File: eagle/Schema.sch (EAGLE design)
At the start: 28 parts, among them T1 2N2222, T2 2N2222

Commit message: Added a led
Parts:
- added LED2: (no value), led:LED5MM
- added R21: (no value), rcl:R-EU_0207/10
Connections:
- new net N$26: R21.2, U$1.12
- new net N$27: LED2.A, R21.1
- new net N$28: LED2.C, U$1.13
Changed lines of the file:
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@@
 <part name="R19" library="rcl" library_urn="urn:adsk.eagle:library:334" deviceset="R-EU_" device="0207/10" package3d_urn="urn:adsk.eagle:package:23491/2"/>
 <part name="R20" library="rcl" library_urn="urn:adsk.eagle:library:334" deviceset="R-EU_" device="0207/10" package3d_urn="urn:adsk.eagle:package:23491/2"/>
+<part name="LED2" library="led" library_urn="urn:adsk.eagle:library:259" deviceset="LED" device="5MM" package3d_urn="urn:adsk.eagle:package:15799/2"/>
+<part name="R21" library="rcl" library_urn="urn:adsk.eagle:library:334" deviceset="R-EU_" device="0207/10" package3d_urn="urn:adsk.eagle:package:23491/2"/>
 </parts>
 <sheets>
@@
 <attribute name="NAME" x="-6.35" y="174.2186" size="1.778" layer="95"/>
 <attribute name="VALUE" x="-6.35" y="169.418" size="1.778" layer="96"/>
+</instance>
+<instance part="LED2" gate="G$1" x="68.58" y="83.82" smashed="yes">
+<attribute name="NAME" x="69.596" y="84.328" size="1.778" layer="95" rot="R90"/>
+<attribute name="VALUE" x="74.295" y="79.248" size="1.778" layer="96" rot="R90"/>
+</instance>
+<instance part="R21" gate="G$1" x="73.66" y="88.9" smashed="yes">
+<attribute name="NAME" x="69.85" y="90.3986" size="1.778" layer="95"/>
+<attribute name="VALUE" x="69.85" y="85.598" size="1.778" layer="96"/>
 </instance>
 </instances>
@@
 </segment>
 </net>
+<net name="N$26" class="0">
+<segment>
+<pinref part="U$1" gate="G$1" pin="12"/>
+<pinref part="R21" gate="G$1" pin="2"/>
+<wire x1="86.36" y1="88.9" x2="78.74" y2="88.9" width="0.1524" layer="91"/>
+</segment>
+</net>
+<net name="N$27" class="0">
+<segment>
+<pinref part="R21" gate="G$1" pin="1"/>
+<pinref part="LED2" gate="G$1" pin="A"/>
+<wire x1="68.58" y1="88.9" x2="68.58" y2="86.36" width="0.1524" layer="91"/>
+</segment>
+</net>
+<net name="N$28" class="0">
+<segment>
+<pinref part="U$1" gate="G$1" pin="13"/>
+<wire x1="86.36" y1="86.36" x2="76.2" y2="86.36" width="0.1524" layer="91"/>
+<pinref part="LED2" gate="G$1" pin="C"/>
+<wire x1="76.2" y1="86.36" x2="76.2" y2="78.74" width="0.1524" layer="91"/>
+<wire x1="76.2" y1="78.74" x2="68.58" y2="78.74" width="0.1524" layer="91"/>
+</segment>
+</net>

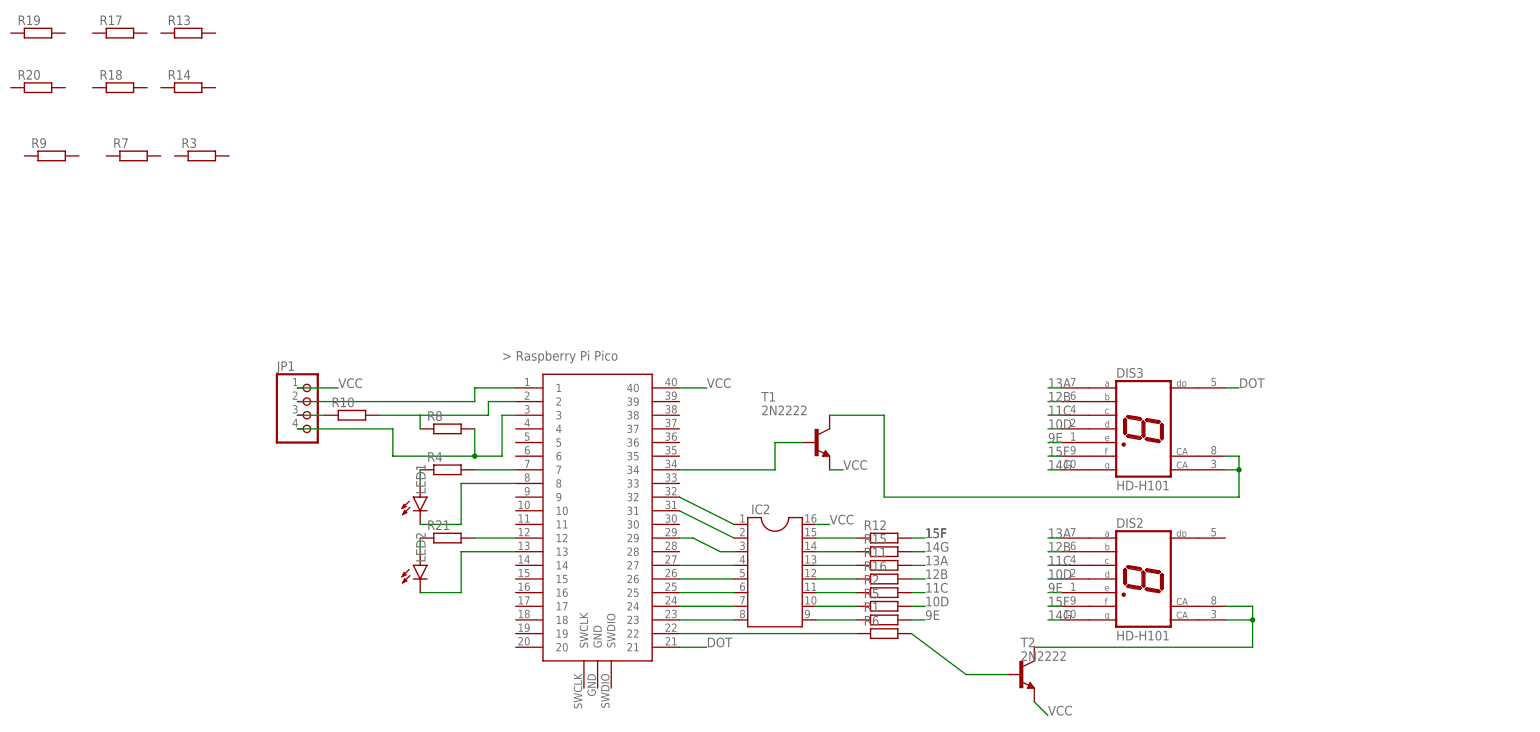
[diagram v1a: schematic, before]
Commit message: [FIX] eagle schéma
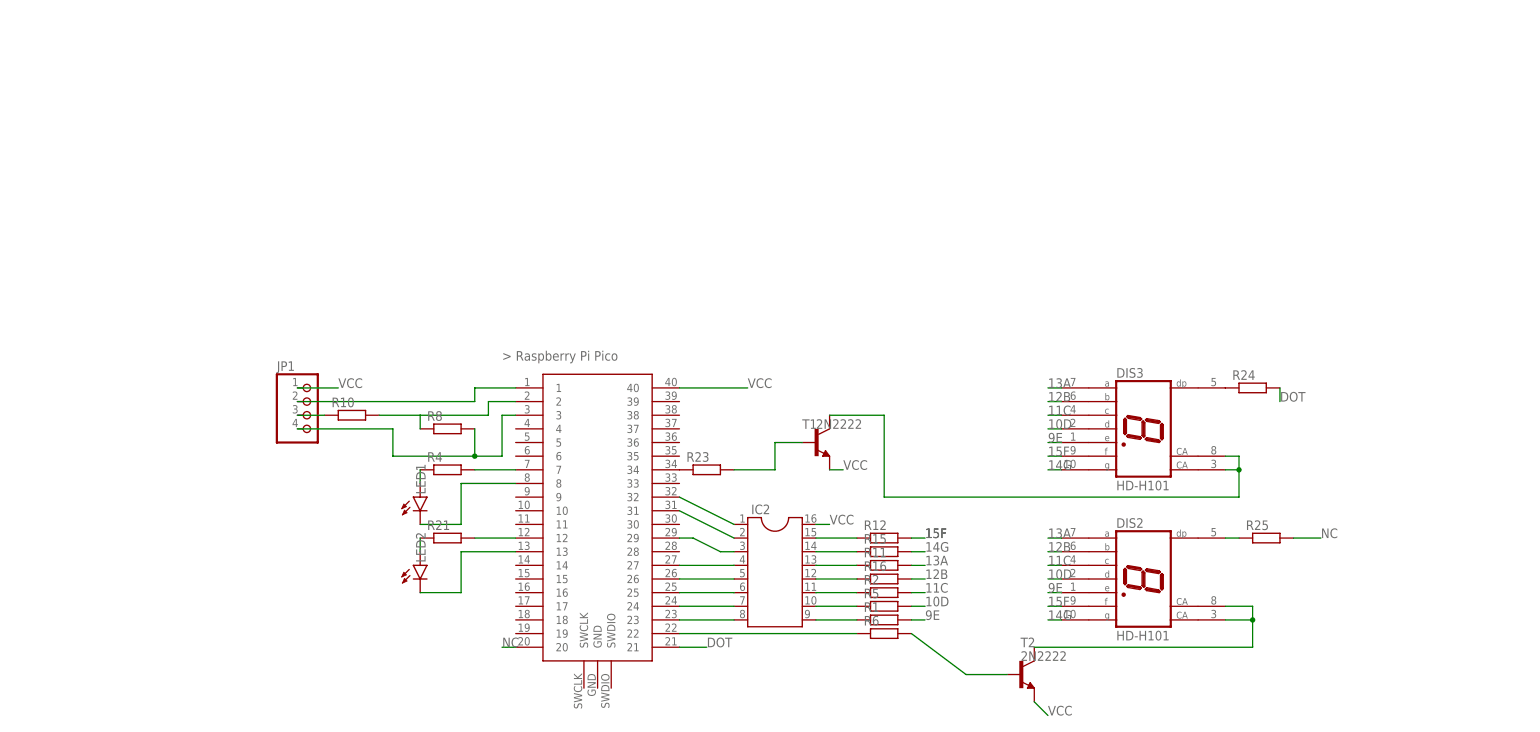
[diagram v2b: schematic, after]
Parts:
- removed R13, R14, R17, R18, R19, R20, R3, R7, R9: (no value), rcl:R-EU_0207/10
- added R23, R24, R25: (no value), rcl:R-EU_0207/10
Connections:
- new net N$32: R23.1, U$1.34
- new net N$33: DIS3.DP, R24.1
- new net N$34: DIS2.DP, R25.1
- new net NC: R25.2, U$1.20
- net DOT: now also R24.2; no longer DIS3.DP
- net N$24: now also R23.2; no longer U$1.34

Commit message: Change to Schema
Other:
- moved on the sheet: R25
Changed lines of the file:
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@@
 <attribute name="VALUE" x="219.71" y="113.538" size="1.778" layer="96"/>
 </instance>
-<instance part="R25" gate="G$1" x="226.06" y="88.9" smashed="yes">
-<attribute name="NAME" x="222.25" y="90.3986" size="1.778" layer="95"/>
-<attribute name="VALUE" x="222.25" y="85.598" size="1.778" layer="96"/>
+<instance part="R25" gate="G$1" x="223.52" y="88.9" smashed="yes">
+<attribute name="NAME" x="219.71" y="90.3986" size="1.778" layer="95"/>
+<attribute name="VALUE" x="219.71" y="85.598" size="1.778" layer="96"/>
 </instance>
 </instances>
@@
 </segment>
 </net>
-<net name="N$34" class="0">
-<segment>
-<pinref part="DIS2" gate="M" pin="DP"/>
-<wire x1="218.44" y1="88.9" x2="220.98" y2="88.9" width="0.1524" layer="91"/>
-<pinref part="R25" gate="G$1" pin="1"/>
-</segment>
-</net>
 <net name="NC" class="0">
 <segment>
@@
 <segment>
 <pinref part="R25" gate="G$1" pin="2"/>
-<wire x1="231.14" y1="88.9" x2="236.22" y2="88.9" width="0.1524" layer="91"/>
+<wire x1="228.6" y1="88.9" x2="236.22" y2="88.9" width="0.1524" layer="91"/>
 <label x="236.22" y="88.9" size="1.778" layer="95"/>
 </segment>
 </net>
+<net name="N$31" class="0">
+<segment>
+<pinref part="DIS2" gate="M" pin="DP"/>
+<pinref part="R25" gate="G$1" pin="1"/>
+</segment>
+</net>

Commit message: changes
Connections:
- removed net N$32: R23.1, U$1.34
- removed net NC: R25.2, U$1.20
- new net 19TOTR: R23.1, U$1.19
- net DOT: now also U$1.20; no longer U$1.21
- net N$1: now also IC2.8; no longer R6.1
- net N$18: now also R6.1, U$1.21; no longer IC2.8, U$1.23
- net VCC: now also R25.2
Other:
- moved on the sheet: R23, T1
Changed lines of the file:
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@@
 <attribute name="VALUE" x="41.91" y="104.14" size="1.778" layer="96"/>
 </instance>
-<instance part="T1" gate="G$1" x="142.24" y="106.68" smashed="yes">
-<attribute name="NAME" x="139.7" y="109.22" size="1.778" layer="95"/>
-<attribute name="VALUE" x="142.24" y="109.22" size="1.778" layer="96"/>
+<instance part="T1" gate="G$1" x="256.54" y="104.14" smashed="yes">
+<attribute name="NAME" x="254" y="106.68" size="1.778" layer="95"/>
+<attribute name="VALUE" x="256.54" y="106.68" size="1.778" layer="96"/>
 </instance>
 <instance part="U$1" gate="G$1" x="101.6" y="91.44" smashed="yes"/>
@@
 <attribute name="VALUE" x="69.85" y="85.598" size="1.778" layer="96"/>
 </instance>
-<instance part="R23" gate="G$1" x="121.92" y="101.6" smashed="yes">
-<attribute name="NAME" x="118.11" y="103.0986" size="1.778" layer="95"/>
-<attribute name="VALUE" x="118.11" y="98.298" size="1.778" layer="96"/>
+<instance part="R23" gate="G$1" x="248.92" y="104.14" smashed="yes">
+<attribute name="NAME" x="245.11" y="105.6386" size="1.778" layer="95"/>
+<attribute name="VALUE" x="245.11" y="100.838" size="1.778" layer="96"/>
 </instance>
 <instance part="R24" gate="G$1" x="223.52" y="116.84" smashed="yes">
@@
 </segment>
 </net>
-<net name="N$18" class="0">
-<segment>
-<pinref part="U$1" gate="G$1" pin="23"/>
-<pinref part="IC2" gate="G$1" pin="8"/>
-<wire x1="116.84" y1="73.66" x2="127" y2="73.66" width="0.1524" layer="91"/>
-</segment>
-</net>
-<net name="N$9" class="0">
-<segment>
-<pinref part="U$1" gate="G$1" pin="32"/>
-<pinref part="IC2" gate="G$1" pin="1"/>
-<wire x1="116.84" y1="96.52" x2="127" y2="91.44" width="0.1524" layer="91"/>
-</segment>
-</net>
-<net name="N$10" class="0">
-<segment>
-<pinref part="U$1" gate="G$1" pin="31"/>
-<pinref part="IC2" gate="G$1" pin="2"/>
-<wire x1="116.84" y1="93.98" x2="127" y2="88.9" width="0.1524" layer="91"/>
-</segment>
-</net>
 <net name="N$11" class="0">
 <segment>
@@
 <segment>
 <pinref part="T1" gate="G$1" pin="E"/>
-<wire x1="144.78" y1="101.6" x2="147.32" y2="101.6" width="0.1524" layer="91"/>
-<label x="147.32" y="101.6" size="1.778" layer="95"/>
+<wire x1="259.08" y1="99.06" x2="269.24" y2="93.98" width="0.1524" layer="91"/>
+<label x="269.24" y="93.98" size="1.778" layer="95"/>
 </segment>
 <segment>
@@
 <wire x1="116.84" y1="116.84" x2="129.54" y2="116.84" width="0.1524" layer="91"/>
 </segment>
-</net>
-<net name="N$1" class="0">
-<segment>
-<pinref part="U$1" gate="G$1" pin="22"/>
-<wire x1="116.84" y1="71.12" x2="149.86" y2="71.12" width="0.1524" layer="91"/>
-<pinref part="R6" gate="G$1" pin="1"/>
+<segment>
+<pinref part="R25" gate="G$1" pin="2"/>
+<wire x1="228.6" y1="88.9" x2="236.22" y2="88.9" width="0.1524" layer="91"/>
+<label x="236.22" y="88.9" size="1.778" layer="95"/>
 </segment>
 </net>
@@
 <net name="N$24" class="0">
 <segment>
-<wire x1="134.62" y1="101.6" x2="134.62" y2="106.68" width="0.1524" layer="91"/>
 <pinref part="T1" gate="G$1" pin="B"/>
-<wire x1="134.62" y1="106.68" x2="139.7" y2="106.68" width="0.1524" layer="91"/>
 <pinref part="R23" gate="G$1" pin="2"/>
-<wire x1="127" y1="101.6" x2="134.62" y2="101.6" width="0.1524" layer="91"/>
 </segment>
 </net>
@@
 <pinref part="DIS3" gate="M" pin="CA"/>
 <wire x1="220.98" y1="101.6" x2="218.44" y2="101.6" width="0.1524" layer="91"/>
+<wire x1="220.98" y1="104.14" x2="220.98" y2="109.22" width="0.1524" layer="91"/>
+<junction x="220.98" y="104.14"/>
 <pinref part="T1" gate="G$1" pin="C"/>
-<wire x1="144.78" y1="111.76" x2="154.94" y2="111.76" width="0.1524" layer="91"/>
-<wire x1="154.94" y1="111.76" x2="154.94" y2="96.52" width="0.1524" layer="91"/>
-<wire x1="154.94" y1="96.52" x2="220.98" y2="96.52" width="0.1524" layer="91"/>
-<wire x1="220.98" y1="96.52" x2="220.98" y2="101.6" width="0.1524" layer="91"/>
-<junction x="220.98" y="101.6"/>
+<wire x1="220.98" y1="109.22" x2="259.08" y2="109.22" width="0.1524" layer="91"/>
 </segment>
 </net>
 <net name="DOT" class="0">
-<segment>
-<pinref part="U$1" gate="G$1" pin="21"/>
-<wire x1="116.84" y1="68.58" x2="121.92" y2="68.58" width="0.1524" layer="91"/>
-<label x="121.92" y="68.58" size="1.778" layer="95"/>
-</segment>
 <segment>
 <pinref part="R24" gate="G$1" pin="2"/>
 <wire x1="228.6" y1="116.84" x2="228.6" y2="114.3" width="0.1524" layer="91"/>
 <label x="228.6" y="114.3" size="1.778" layer="95"/>
+</segment>
+<segment>
+<pinref part="U$1" gate="G$1" pin="20"/>
+<wire x1="86.36" y1="68.58" x2="83.82" y2="68.58" width="0.1524" layer="91"/>
+<label x="83.82" y="68.58" size="1.778" layer="95"/>
 </segment>
 </net>
@@
 </segment>
 </net>
-<net name="N$32" class="0">
-<segment>
-<pinref part="U$1" gate="G$1" pin="34"/>
-<pinref part="R23" gate="G$1" pin="1"/>
-</segment>
-</net>
 <net name="N$33" class="0">
 <segment>
@@
 </segment>
 </net>
-<net name="NC" class="0">
-<segment>
-<pinref part="U$1" gate="G$1" pin="20"/>
-<wire x1="86.36" y1="68.58" x2="83.82" y2="68.58" width="0.1524" layer="91"/>
-<label x="83.82" y="68.58" size="1.778" layer="95"/>
-</segment>
-<segment>
-<pinref part="R25" gate="G$1" pin="2"/>
-<wire x1="228.6" y1="88.9" x2="236.22" y2="88.9" width="0.1524" layer="91"/>
-<label x="236.22" y="88.9" size="1.778" layer="95"/>
-</segment>
-</net>
 <net name="N$31" class="0">
 <segment>
@@
 </segment>
 </net>
+<net name="19TOTR" class="0">
+<segment>
+<pinref part="U$1" gate="G$1" pin="19"/>
+<wire x1="86.36" y1="71.12" x2="83.82" y2="71.12" width="0.1524" layer="91"/>
+<label x="83.82" y="71.12" size="1.778" layer="95"/>
+</segment>
+<segment>
+<pinref part="R23" gate="G$1" pin="1"/>
+<wire x1="243.84" y1="104.14" x2="241.3" y2="104.14" width="0.1524" layer="91"/>
+<label x="241.3" y="104.14" size="1.778" layer="95"/>
+</segment>
+</net>
+<net name="N$9" class="0">
+<segment>
+<pinref part="IC2" gate="G$1" pin="1"/>
+<pinref part="U$1" gate="G$1" pin="32"/>
+<wire x1="127" y1="91.44" x2="127" y2="96.52" width="0.1524" layer="91"/>
+<wire x1="127" y1="96.52" x2="116.84" y2="96.52" width="0.1524" layer="91"/>
+</segment>
+</net>
+<net name="N$10" class="0">
+<segment>
+<pinref part="IC2" gate="G$1" pin="2"/>
+<wire x1="127" y1="88.9" x2="124.46" y2="88.9" width="0.1524" layer="91"/>
+<wire x1="124.46" y1="88.9" x2="124.46" y2="93.98" width="0.1524" layer="91"/>
+<pinref part="U$1" gate="G$1" pin="31"/>
+<wire x1="124.46" y1="93.98" x2="116.84" y2="93.98" width="0.1524" layer="91"/>
+</segment>
+</net>
+<net name="N$1" class="0">
+<segment>
+<pinref part="IC2" gate="G$1" pin="8"/>
+<wire x1="127" y1="73.66" x2="124.46" y2="73.66" width="0.1524" layer="91"/>
+<wire x1="124.46" y1="73.66" x2="124.46" y2="71.12" width="0.1524" layer="91"/>
+<pinref part="U$1" gate="G$1" pin="22"/>
+<wire x1="124.46" y1="71.12" x2="116.84" y2="71.12" width="0.1524" layer="91"/>
+</segment>
+</net>
+<net name="N$18" class="0">
+<segment>
+<pinref part="R6" gate="G$1" pin="1"/>
+<wire x1="149.86" y1="71.12" x2="127" y2="71.12" width="0.1524" layer="91"/>
+<wire x1="127" y1="71.12" x2="127" y2="68.58" width="0.1524" layer="91"/>
+<pinref part="U$1" gate="G$1" pin="21"/>
+<wire x1="127" y1="68.58" x2="116.84" y2="68.58" width="0.1524" layer="91"/>
+</segment>
+</net>

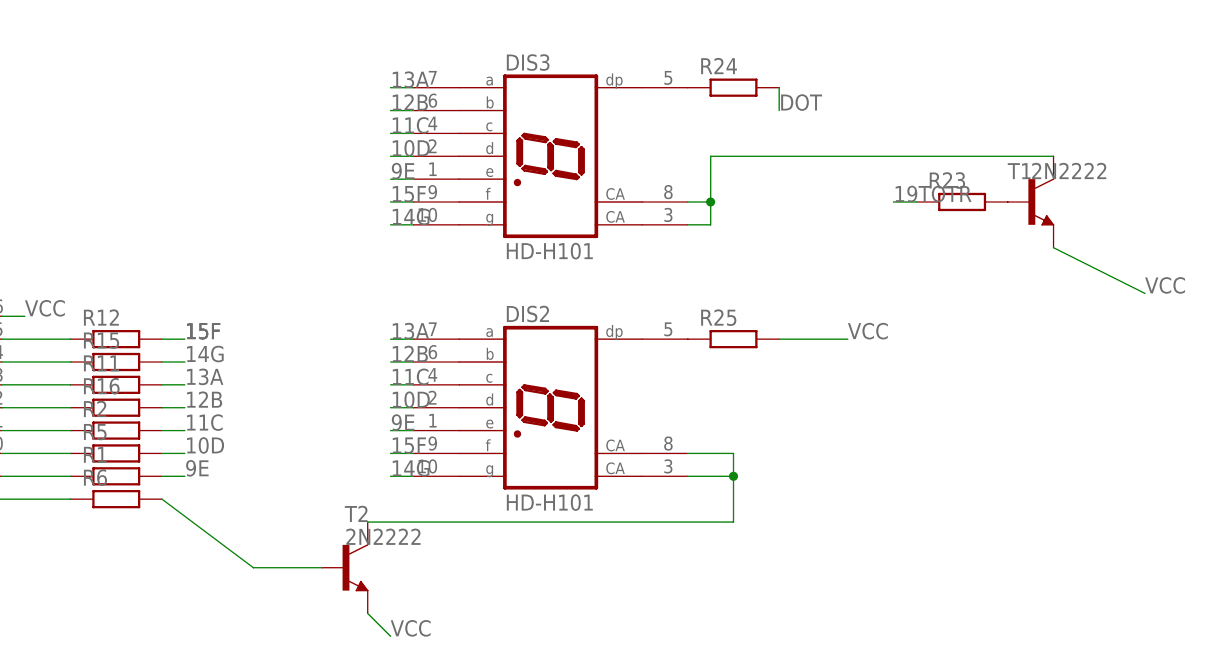
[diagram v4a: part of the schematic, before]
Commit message: [FIX] Transistor flipped
Correction du prof
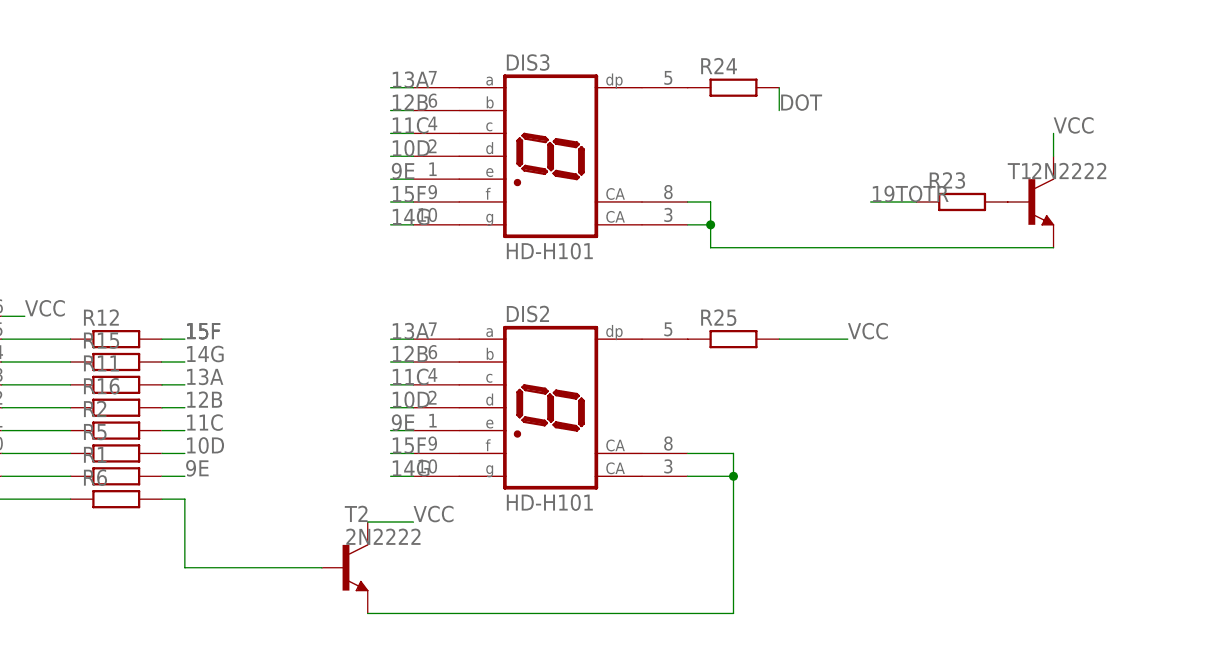
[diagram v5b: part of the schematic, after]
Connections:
- net N$25: now also T1.E; no longer T1.C
- net N$29: now also T2.E; no longer T2.C
- net VCC: now also T1.C, T2.C; no longer T1.E, T2.E
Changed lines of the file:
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@@
 <wire x1="223.52" y1="76.2" x2="223.52" y2="73.66" width="0.1524" layer="91"/>
 <wire x1="223.52" y1="73.66" x2="218.44" y2="73.66" width="0.1524" layer="91"/>
-<pinref part="T2" gate="G$1" pin="C"/>
-<wire x1="182.88" y1="68.58" x2="223.52" y2="68.58" width="0.1524" layer="91"/>
-<wire x1="223.52" y1="68.58" x2="223.52" y2="73.66" width="0.1524" layer="91"/>
 <junction x="223.52" y="73.66"/>
+<pinref part="T2" gate="G$1" pin="E"/>
+<wire x1="182.88" y1="58.42" x2="223.52" y2="58.42" width="0.1524" layer="91"/>
+<wire x1="223.52" y1="58.42" x2="223.52" y2="73.66" width="0.1524" layer="91"/>
 </segment>
 </net>
@@
 </segment>
 <segment>
-<pinref part="T2" gate="G$1" pin="E"/>
-<wire x1="182.88" y1="58.42" x2="185.42" y2="55.88" width="0.1524" layer="91"/>
-<label x="185.42" y="55.88" size="1.778" layer="95"/>
-</segment>
-<segment>
-<pinref part="T1" gate="G$1" pin="E"/>
-<wire x1="259.08" y1="99.06" x2="269.24" y2="93.98" width="0.1524" layer="91"/>
-<label x="269.24" y="93.98" size="1.778" layer="95"/>
-</segment>
-<segment>
 <label x="129.54" y="116.84" size="1.778" layer="95"/>
 <pinref part="U$1" gate="G$1" pin="40"/>
@@
 <label x="236.22" y="88.9" size="1.778" layer="95"/>
 </segment>
-</net>
-<net name="N$30" class="0">
-<segment>
-<pinref part="R6" gate="G$1" pin="2"/>
-<pinref part="T2" gate="G$1" pin="B"/>
-<wire x1="160.02" y1="71.12" x2="170.18" y2="63.5" width="0.1524" layer="91"/>
-<wire x1="170.18" y1="63.5" x2="177.8" y2="63.5" width="0.1524" layer="91"/>
+<segment>
+<pinref part="T2" gate="G$1" pin="C"/>
+<wire x1="182.88" y1="68.58" x2="187.96" y2="68.58" width="0.1524" layer="91"/>
+<label x="187.96" y="68.58" size="1.778" layer="95"/>
+</segment>
+<segment>
+<pinref part="T1" gate="G$1" pin="C"/>
+<wire x1="259.08" y1="109.22" x2="259.08" y2="111.76" width="0.1524" layer="91"/>
+<label x="259.08" y="111.76" size="1.778" layer="95"/>
 </segment>
 </net>
@@
 <pinref part="DIS3" gate="M" pin="CA"/>
 <wire x1="220.98" y1="101.6" x2="218.44" y2="101.6" width="0.1524" layer="91"/>
-<wire x1="220.98" y1="104.14" x2="220.98" y2="109.22" width="0.1524" layer="91"/>
-<junction x="220.98" y="104.14"/>
-<pinref part="T1" gate="G$1" pin="C"/>
-<wire x1="220.98" y1="109.22" x2="259.08" y2="109.22" width="0.1524" layer="91"/>
+<wire x1="220.98" y1="101.6" x2="220.98" y2="99.06" width="0.1524" layer="91"/>
+<junction x="220.98" y="101.6"/>
+<pinref part="T1" gate="G$1" pin="E"/>
+<wire x1="220.98" y1="99.06" x2="259.08" y2="99.06" width="0.1524" layer="91"/>
 </segment>
 </net>
@@
 <segment>
 <pinref part="R23" gate="G$1" pin="1"/>
-<wire x1="243.84" y1="104.14" x2="241.3" y2="104.14" width="0.1524" layer="91"/>
-<label x="241.3" y="104.14" size="1.778" layer="95"/>
+<wire x1="243.84" y1="104.14" x2="238.76" y2="104.14" width="0.1524" layer="91"/>
+<label x="238.76" y="104.14" size="1.778" layer="95"/>
 </segment>
 </net>
@@
 </segment>
 </net>
+<net name="N$30" class="0">
+<segment>
+<pinref part="R6" gate="G$1" pin="2"/>
+<wire x1="160.02" y1="71.12" x2="162.56" y2="71.12" width="0.1524" layer="91"/>
+<wire x1="162.56" y1="71.12" x2="162.56" y2="63.5" width="0.1524" layer="91"/>
+<pinref part="T2" gate="G$1" pin="B"/>
+<wire x1="162.56" y1="63.5" x2="177.8" y2="63.5" width="0.1524" layer="91"/>
+</segment>
+</net>
